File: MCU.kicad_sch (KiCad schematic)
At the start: 13 parts, among them J1 Conn_ARM_SWD_TagConnect_TC203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, SW1 SW_000001, SW2 SW_000001, U1 NORA-B106-00B, Y2 CLK_0002

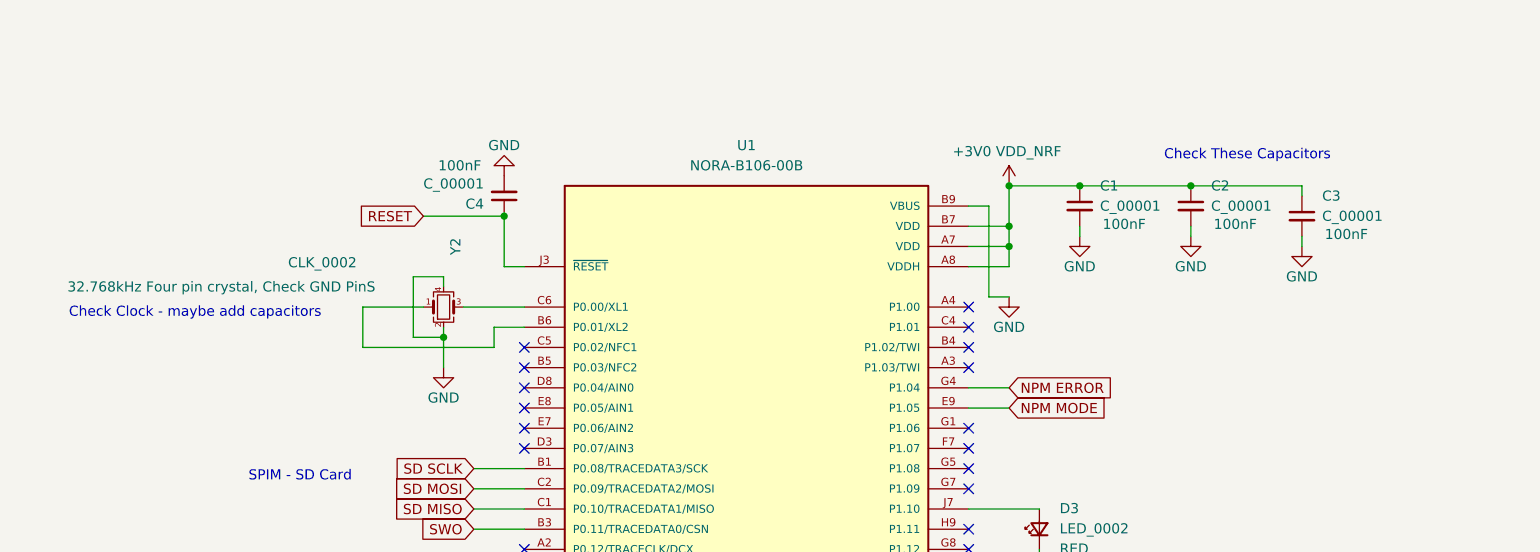
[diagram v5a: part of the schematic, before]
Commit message: added schmatic symbols and footprints for key capacitors, selected LCXO crystal to use internal caps
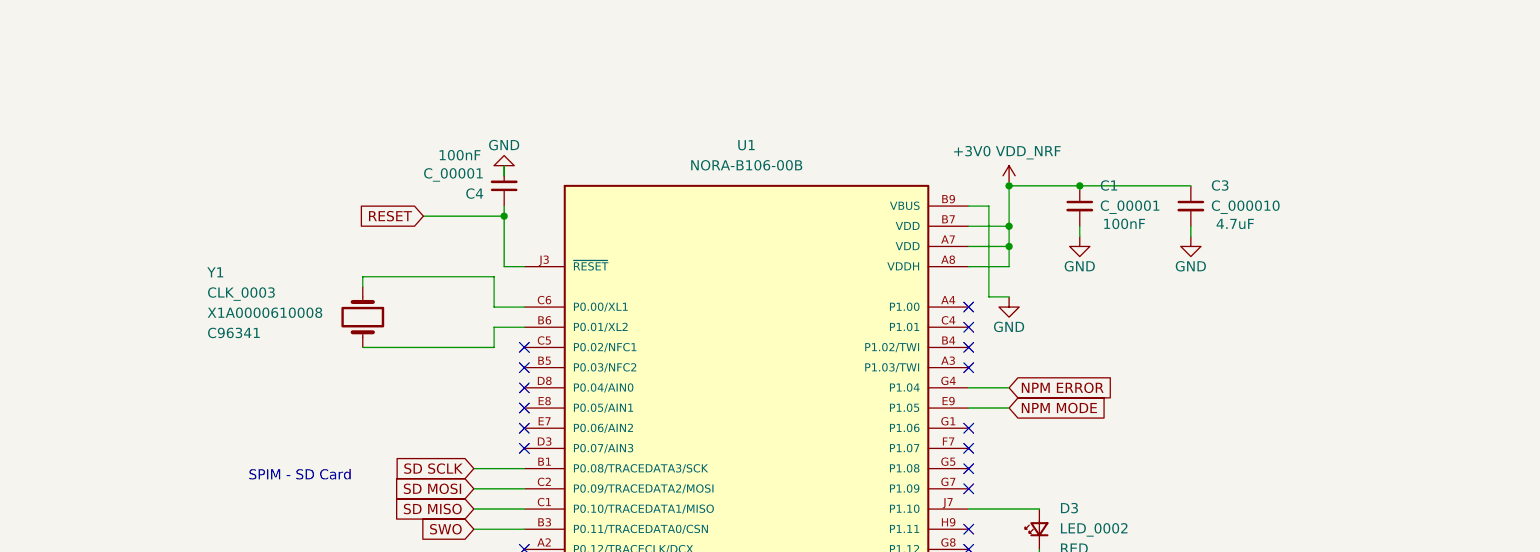
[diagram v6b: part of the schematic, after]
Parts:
- removed C2, C3: C_00001, symbol mic_patch_parts:C_00001
- removed Y2: CLK_0002, symbol mic_patch_parts:CLK_0002
- added C3: C_000010, Capacitor_SMD:C_0402_1005Metric, symbol mic_patch_parts:C_000010
- added Y1: CLK_0003, Crystal:Crystal_SMD_2012-2Pin_2.0x1.2mm, symbol mic_patch_parts:CLK_0003
- C1, C4: footprint (none) -> Capacitor_SMD:C_0402_1005Metric; LCSC PNs (none) -> C25744; MPNs (none) -> 0402WGF1002TCE
- R11, R13, R14: footprint (none) -> Resistor_SMD:R_0402_1005Metric; LCSC PNs (none) -> C25744; MPNs (none) -> 0402WGF1002TCE
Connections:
- net +3V0 VDD_NRF: now also C3.1
- net GND: now also C3.2
- net at U1.B6 (P0.01/XL2): now also Y1.2
- net at U1.C6 (P0.00/XL1): now also Y1.1
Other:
- note removed: "Check Clock - maybe add capacitors"
- note removed: "Check These Capacitors"
- moved on the sheet: C4

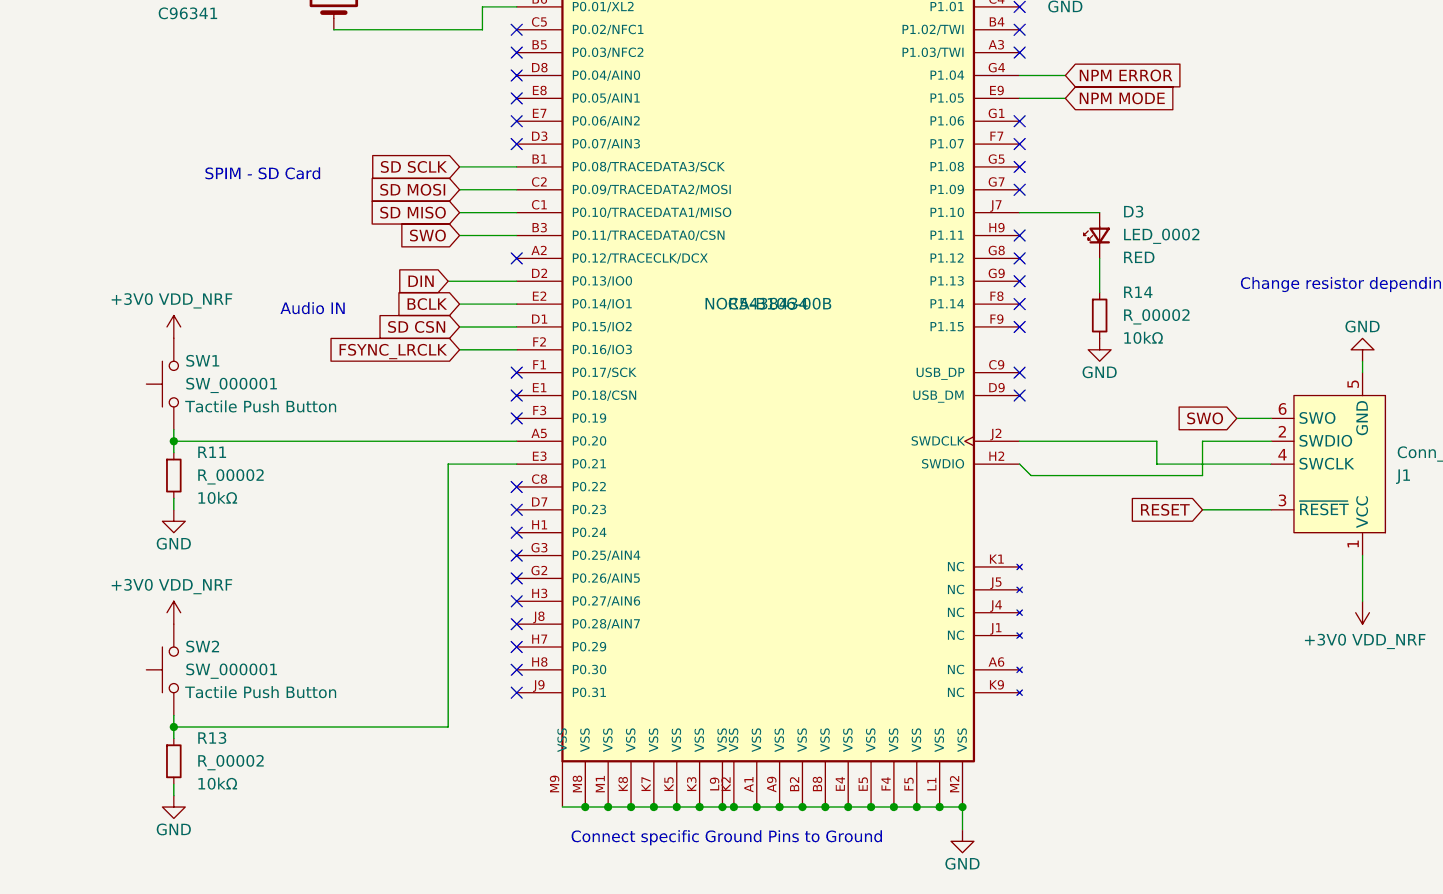
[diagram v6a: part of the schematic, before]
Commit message: added SMD indicator LED symbol & footprint
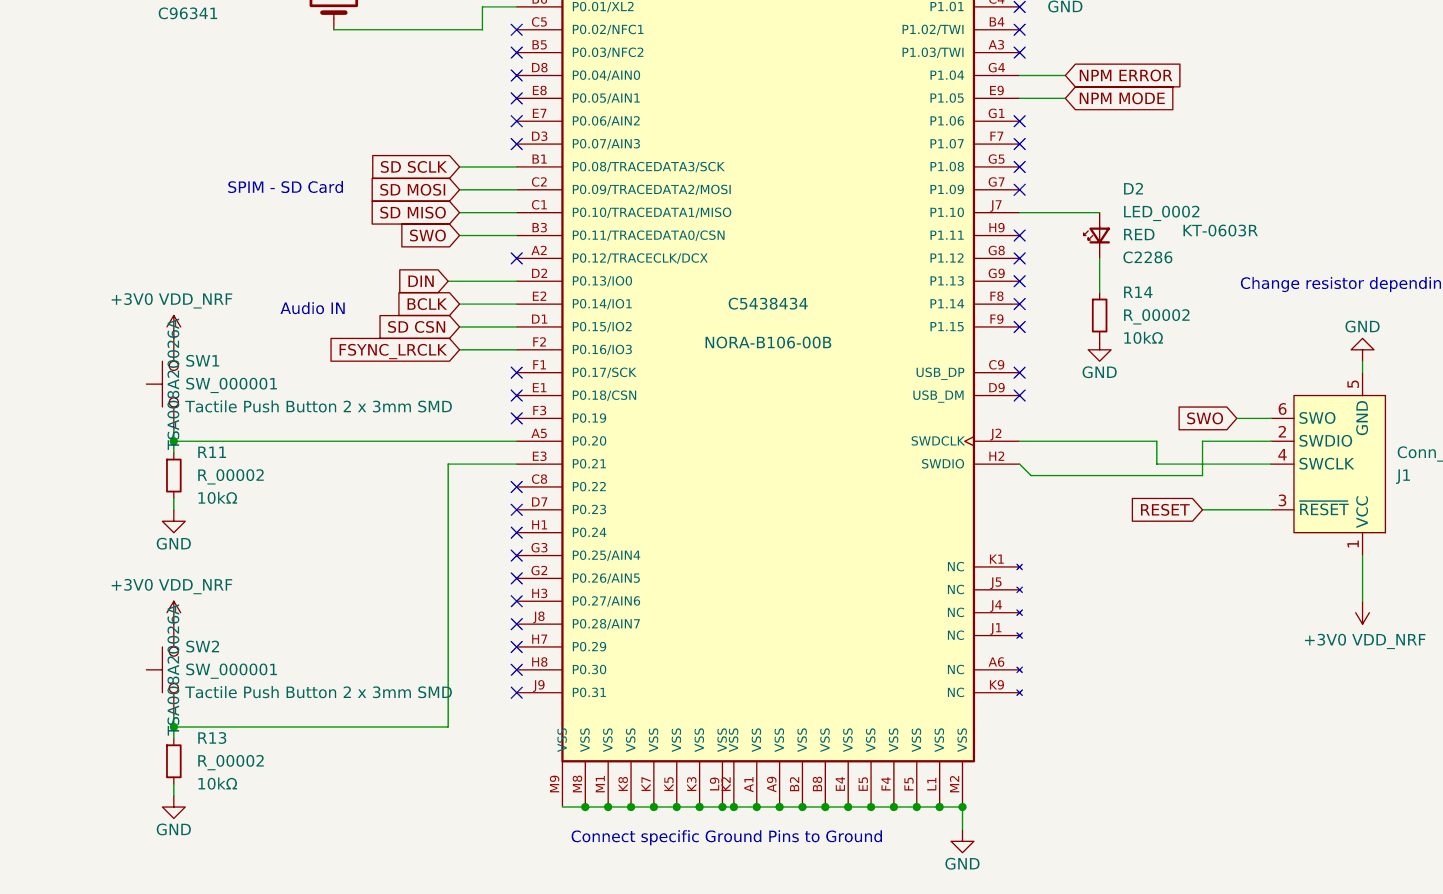
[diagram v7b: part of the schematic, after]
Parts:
- removed D3: LED_0002, symbol mic_patch_parts:LED_0003
- added D2: LED_0002, LED_SMD:LED_0603_1608Metric, symbol mic_patch_parts:LED_0002
- SW1, SW2: footprint (none) -> mic_patch_parts:SW_000001; Desc Tactile Push Button -> Tactile Push Button 2 x 3mm SMD; LCSC PNs (none) -> C2888880; MPNs (none) -> TSA008A20026A
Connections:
- net at U1.J7 (P1.10): now also D2.2 (A)
- net at R14.1: now also D2.1 (K)
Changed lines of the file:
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@@
 	(text "SPIM - SD Card"
 		(exclude_from_sim no)
-		(at 58.166 100.076 0)
+		(at 60.706 101.6 0)
 		(effects
 			(font
@@
 	)
 	(symbol
+		(lib_id "mic_patch_parts:LED_0002")
+		(at 151.13 106.68 90)
+		(unit 1)
+		(exclude_from_sim no)
+		(in_bom yes)
+		(on_board yes)
+		(dnp no)
+		(property "Reference" "D2"
+			(at 153.67 101.5364 90)
+			(effects
+				(font
+					(size 1.27 1.27)
+				)
+				(justify right)
+			)
+		)
+		(property "Value" "LED_0002"
+			(at 153.67 104.0764 90)
+			(effects
+				(font
+					(size 1.27 1.27)
+				)
+				(justify right)
+			)
+		)
+		(property "Footprint" "LED_SMD:LED_0603_1608Metric"
+			(at 151.13 106.68 90)
+			(effects
+				(font
+					(size 1.27 1.27)
+				)
+				(hide yes)
+			)
+		)
+		(property "Datasheet" "~"
+			(at 151.13 106.68 90)
+			(effects
+				(font
+					(size 1.27 1.27)
+				)
+				(hide yes)
+			)
+		)
+		(property "Description" "RED LED"
+			(at 147.828 108.712 0)
+			(effects
+				(font
+					(size 1.27 1.27)
+				)
+				(hide yes)
+			)
+		)
+		(property "Desc" "RED"
+			(at 153.67 106.6164 90)
+			(effects
+				(font
+					(size 1.27 1.27)
+				)
+				(justify right)
+			)
+		)
+		(property "LCSC PNs" "C2286"
+			(at 153.67 109.1564 90)
+			(effects
+				(font
+					(size 1.27 1.27)
+				)
+				(justify right)
+			)
+		)
+		(property "MFN PNS" "KT-0603R"
+			(at 160.274 106.172 90)
+			(effects
+				(font
+					(size 1.27 1.27)
+				)
+				(justify right)
+			)
+		)
+		(pin "2"
+		)
+		(pin "1"
+		)
+		(instances
+			(project "mic_patch_v1"
+				(path "/5448a297-4261-40a5-8009-47199bfe22cb/1e8f7a85-c9d9-4dea-908a-5a79456d7ca4"
+					(reference "D2")
+					(unit 1)
+				)
+			)
+		)
+	)
+	(symbol
 		(lib_id "power:GND")
 		(at 170.18 69.85 0)
@@
 			)
 		)
-		(property "Footprint" ""
+		(property "Footprint" "mic_patch_parts:SW_000001"
 			(at 43.18 123.19 0)
 			(effects
@@
 			)
 		)
-		(property "LCSC PNs" ""
+		(property "LCSC PNs" "C2888880"
 			(at 33.782 123.19 0)
 			(effects
@@
 			)
 		)
-		(property "Desc" "Tactile Push Button"
+		(property "Desc" "Tactile Push Button 2 x 3mm SMD"
 			(at 49.53 125.7299 90)
 			(effects
@@
 				)
 				(justify right)
+			)
+		)
+		(property "MPNs" "TSA008A20026A "
+			(at 48.26 123.19 0)
+			(effects
+				(font
+					(size 1.27 1.27)
+				)
 			)
 		)
@@
 		(on_board yes)
 		(dnp no)
-		(fields_autoplaced yes)
 		(property "Reference" "U1"
 			(at 114.3 58.42 0)
@@
 		)
 		(property "MPNS" "NORA-B106-00B"
-			(at 114.3 114.3 0)
+			(at 114.3 118.618 0)
 			(effects
 				(font
@@
 	)
 	(symbol
-		(lib_id "mic_patch_parts:LED_0003")
-		(at 151.13 106.68 90)
-		(unit 1)
-		(exclude_from_sim no)
-		(in_bom yes)
-		(on_board yes)
-		(dnp no)
-		(fields_autoplaced yes)
-		(property "Reference" "D3"
-			(at 153.67 104.0764 90)
-			(effects
-				(font
-					(size 1.27 1.27)
-				)
-				(justify right)
-			)
-		)
-		(property "Value" "LED_0002"
-			(at 153.67 106.6164 90)
-			(effects
-				(font
-					(size 1.27 1.27)
-				)
-				(justify right)
-			)
-		)
-		(property "Footprint" ""
-			(at 151.13 106.68 90)
-			(effects
-				(font
-					(size 1.27 1.27)
-				)
-				(hide yes)
-			)
-		)
-		(property "Datasheet" "~"
-			(at 151.13 106.68 90)
-			(effects
-				(font
-					(size 1.27 1.27)
-				)
-				(hide yes)
-			)
-		)
-		(property "Description" "RED LED"
-			(at 147.828 108.712 0)
-			(effects
-				(font
-					(size 1.27 1.27)
-				)
-				(hide yes)
-			)
-		)
-		(property "Desc" "RED"
-			(at 153.67 109.1564 90)
-			(effects
-				(font
-					(size 1.27 1.27)
-				)
-				(justify right)
-			)
-		)
-		(pin "2"
-		)
-		(pin "1"
-		)
-		(instances
-			(project "mic_patch_v1"
-				(path "/5448a297-4261-40a5-8009-47199bfe22cb/1e8f7a85-c9d9-4dea-908a-5a79456d7ca4"
-					(reference "D3")
-					(unit 1)
-				)
-			)
-		)
-	)
-	(symbol
 		(lib_id "power:GND")
 		(at 147.32 77.47 0)
@@
 			)
 		)
-		(property "Footprint" ""
+		(property "Footprint" "mic_patch_parts:SW_000001"
 			(at 43.18 154.94 0)
 			(effects
@@
 			)
 		)
-		(property "LCSC PNs" ""
+		(property "LCSC PNs" "C2888880"
 			(at 33.782 154.94 0)
 			(effects
@@
 			)
 		)
-		(property "Desc" "Tactile Push Button"
+		(property "Desc" "Tactile Push Button 2 x 3mm SMD"
 			(at 49.53 157.4799 90)
 			(effects
@@
 			)
 		)
+		(property "MPNs" "TSA008A20026A "
+			(at 48.26 154.94 0)
+			(effects
+				(font
+					(size 1.27 1.27)
+				)
+			)
+		)

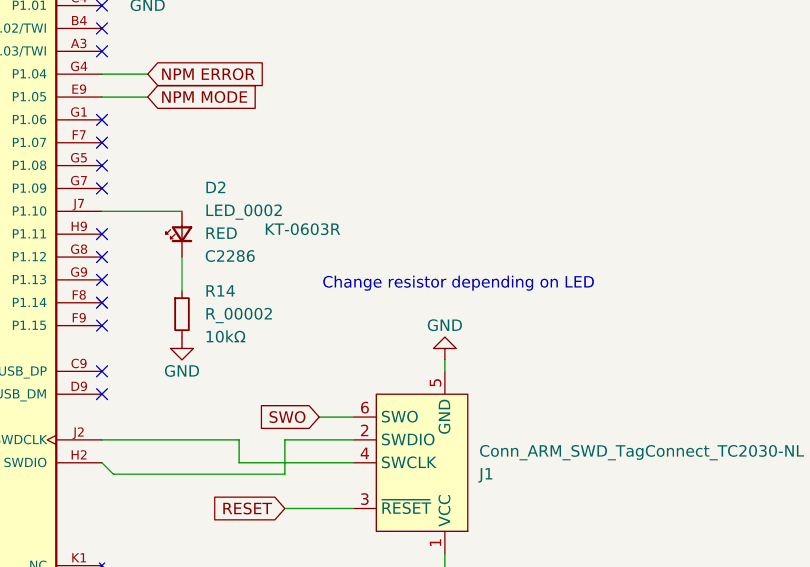
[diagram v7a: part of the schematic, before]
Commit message: added JST connector symbol + footprint
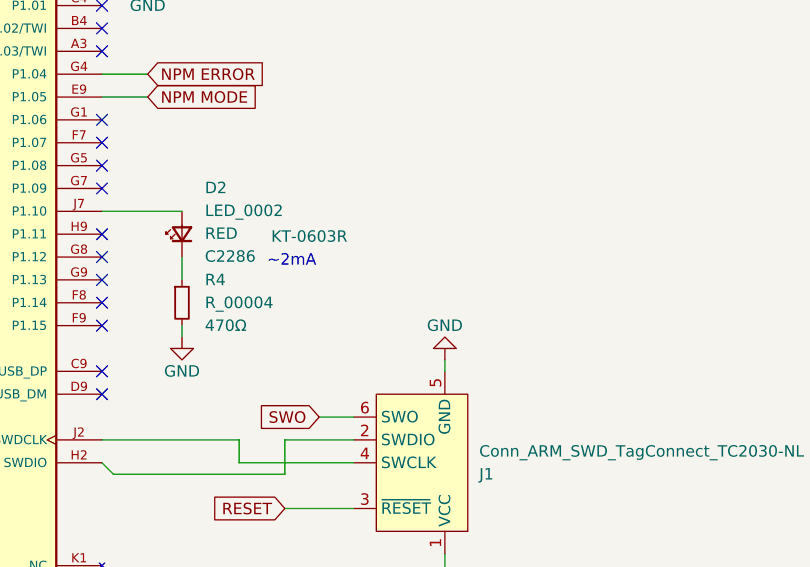
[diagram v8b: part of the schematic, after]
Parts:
- removed R14: R_00002, Resistor_SMD:R_0402_1005Metric, symbol mic_patch_parts:R_00003
- added R4: R_00004, Resistor_SMD:R_0402_1005Metric, symbol mic_patch_parts:R_00004
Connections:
- net GND: now also R4.2
- net at D2.1 (K): now also R4.1
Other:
- note added: "~2mA"
- note removed: "Change resistor depending on LED"
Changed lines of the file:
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@@
 	(wire
 		(pts
-			(xy 151.13 109.22) (xy 151.13 113.03)
+			(xy 151.13 109.22) (xy 151.13 111.76)
 		)
 		(stroke
@@
 		(pts
 			(xy 144.78 77.47) (xy 147.32 77.47)
+		)
+		(stroke
+			(width 0)
+			(type default)
+		)
+	)
+	(wire
+		(pts
+			(xy 151.13 116.84) (xy 151.13 118.11)
 		)
 		(stroke
@@
 		)
 	)
-	(text "Change resistor depending on LED"
-		(exclude_from_sim no)
-		(at 181.864 112.268 0)
+	(text "~2mA"
+		(exclude_from_sim no)
+		(at 163.322 109.728 0)
 		(effects
 			(font
@@
 		)
 		(property "MFN PNS" "KT-0603R"
-			(at 160.274 106.172 90)
+			(at 161.036 106.934 90)
 			(effects
 				(font
@@
 	)
 	(symbol
-		(lib_id "mic_patch_parts:R_00003")
-		(at 151.13 115.57 0)
+		(lib_id "mic_patch_parts:R_00004")
+		(at 151.13 114.3 0)
 		(unit 1)
 		(exclude_from_sim no)
@@
 		(dnp no)
 		(fields_autoplaced yes)
-		(property "Reference" "R14"
-			(at 153.67 113.0299 0)
+		(property "Reference" "R4"
+			(at 153.67 111.7599 0)
 			(effects
 				(font
@@
 			)
 		)
-		(property "Value" "R_00002"
-			(at 153.67 115.5699 0)
+		(property "Value" "R_00004"
+			(at 153.67 114.2999 0)
 			(effects
 				(font
@@
 		)
 		(property "Footprint" "Resistor_SMD:R_0402_1005Metric"
-			(at 151.13 115.57 0)
+			(at 151.13 114.3 0)
 			(effects
 				(font
@@
 		)
 		(property "Datasheet" "~"
-			(at 151.13 115.57 0)
-			(effects
-				(font
-					(size 1.27 1.27)
-				)
-				(hide yes)
-			)
-		)
-		(property "Description" "10kΩ resistor 0402"
-			(at 151.13 115.57 0)
-			(effects
-				(font
-					(size 1.27 1.27)
-				)
-				(hide yes)
-			)
-		)
-		(property "Desc" "10kΩ "
-			(at 153.67 118.1099 0)
+			(at 151.13 114.3 0)
+			(effects
+				(font
+					(size 1.27 1.27)
+				)
+				(hide yes)
+			)
+		)
+		(property "Description" "470Ω resistor"
+			(at 151.13 114.3 0)
+			(effects
+				(font
+					(size 1.27 1.27)
+				)
+				(hide yes)
+			)
+		)
+		(property "Desc" "470Ω "
+			(at 153.67 116.8399 0)
 			(effects
 				(font
@@
 			)
 		)
-		(property "MPNs" "0402WGF1002TCE"
-			(at 151.13 115.57 0)
-			(effects
-				(font
-					(size 1.27 1.27)
-				)
-				(hide yes)
-			)
-		)
-		(property "LCSC PNs" "C25744"
-			(at 151.13 115.57 0)
-			(effects
-				(font
-					(size 1.27 1.27)
-				)
-				(hide yes)
-			)
+		(property "MPNs" "0402WGF4700TCE"
+			(at 151.13 114.3 0)
+			(effects
+				(font
+					(size 1.27 1.27)
+				)
+				(hide yes)
+			)
+		)
+		(property "LCSC PNs" "C25117"
+			(at 151.13 114.3 0)
+			(effects
+				(font
+					(size 1.27 1.27)
+				)
+				(hide yes)
+			)
+		)
+		(pin "1"
 		)
 		(pin "2"
-		)
-		(pin "1"
 		)
 		(instances
 			(project "mic_patch_v1"
 				(path "/5448a297-4261-40a5-8009-47199bfe22cb/1e8f7a85-c9d9-4dea-908a-5a79456d7ca4"
-					(reference "R14")
+					(reference "R4")
 					(unit 1)
 				)
